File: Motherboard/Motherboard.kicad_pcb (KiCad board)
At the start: 8 copper layers, 304.8 x 243.8 mm, 102 parts, among them J1 ATX-20, J2 65SIB_Connector, J3 DB9_Header, J4 GPIO_Connector, J5 Expansion_Connector, J6 Expansion_Connector, J7 Expansion_Connector, J8 Expansion_Connector, J9 Expansion_Connector, SW1 SW_SPST, U1 74HCT138, U10 74HCT138, U2 AS6C4008-55PCN, U3 74HCT138, U4 74HCT138, U5 74HCT138, U6 28C010, U7 74HCT08, U8 74HCT138, U9 74HCT138, X1 ACO-8MHz

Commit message: 406 traces left to route...
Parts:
- added C3: 100 nF, Capacitor_THT:C_Disc_D3.0mm_W1.6mm_P2.50mm, F.Cu at (160.0, 108.0)
- added U11: 74HCT02, Package_DIP:DIP-14_W7.62mm_Socket_LongPads, F.Cu at (154.9, 114.3)
- J4: footprint Connector_PinSocket_2.54mm:PinSocket_2x11_P2.54mm_Vertical -> Connector_PinHeader_2.54mm:PinHeader_2x11_P2.54mm_Vertical
- moved J4 32.5 mm to (297.2, 223.5)
- renumbered NOR1 to NOT1
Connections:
- U10 pad 11: unconnected-(U10-Pad11) -> ~{CS_65SIB}
- U10 pad 13: ~{CS_65SIB} -> unconnected-(U10-Pad13)
- U2 pad 1: ROM4_EN -> RAM4_EN
- U2 pad 2: ROM2_EN -> RAM2_EN
- U2 pad 30: ROM3_EN -> RAM3_EN
- U2 pad 31: ROM1_EN -> RAM1_EN
- U4 pad 5: GND -> A7
- U4 pad 6: A7 -> VCC
- U7 pad 4: Net-(U7-Pad4) -> (no net)
- U7 pad 5: Net-(U7-Pad5) -> (no net)
- U7 pad 6: CS_DEV -> (no net)
- ~CS_DEV1 pad 10: Net-(U7-Pad5) -> Net-(U11-Pad3)
- ~CS_DEV2 pad 15: Net-(U7-Pad4) -> Net-(U11-Pad2)
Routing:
- net ~{IRQ1}: track 55.9 -> 411.3 mm, vias 1 -> 3
- net CLK: track 129.5 -> 375.8 mm, vias 3 -> 5
- net R\~{W}: track 39.4 -> 229.9 mm, vias 1 -> 2
- net A0: track 67.5 -> 223.1 mm, vias 1 -> 2
- net MEM_D0: track 158.0 -> 264.3 mm
- net MEM_D2: track 157.8 -> 263.8 mm
- net MEM_D1: track 157.9 -> 263.8 mm
- net PHI2: track 67.3 -> 139.5 mm, vias 2 -> 3
- net A3: track 63.7 -> 132.3 mm, vias 1 -> 2
- net A2: track 65.3 -> 127.5 mm, vias 1 -> 2
- net Net-(U11-Pad3): track 0.00 -> 62.2 mm, vias 0 -> 2
- net A1: track 66.2 -> 122.1 mm, vias 1 -> 2
- net VCC: track 1422.6 -> 1478.1 mm
- net CA1: track 37.3 -> 0.00 mm
- net CA2: track 33.5 -> 0.00 mm
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
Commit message: 405 unrouted traces...
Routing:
- net GPIO9: track 7.67 -> 0.00 mm
- net RAM1_EN: track 1.27 -> 0.00 mm
- net ROM4_EN: track 0.77 -> 0.00 mm
- net GND: track 1607.3 -> 1606.8 mm
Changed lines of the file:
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@@
   (segment (start 165.11 86.365) (end 165.11 96.525) (width 0.25) (layer "F.Cu") (net 1))
   (segment (start 102.88 96.51) (end 102.88 93.97) (width 0.25) (layer "F.Cu") (net 1))
-  (segment (start 119.39 124.45) (end 119.89904 124.45) (width 0.25) (layer "F.Cu") (net 1))
   (segment (start 162.575 99.06) (end 140.97 99.06) (width 0.25) (layer "F.Cu") (net 1))
   (segment (start 77.48 34.3) (end 61.17 34.3) (width 0.25) (layer "F.Cu") (net 1))
@@
   (segment (start 133.505489 210.664511) (end 143.625489 210.664511) (width 0.25) (layer "In3.Cu") (net 1))
   (segment (start 219.705 177.8) (end 220.829511 178.924511) (width 0.25) (layer "In3.Cu") (net 1))
-  (segment (start 234.95 143.51) (end 234.945 143.505) (width 0.25) (layer "F.Cu") (net 2))
-  (segment (start 234.945 143.505) (end 234.945 142.24) (width 0.25) (layer "F.Cu") (net 2))
-  (segment (start 265.43 141.6975) (end 264.8875 142.24) (width 0.25) (layer "In3.Cu") (net 9))
   (segment (start 251.46 110.49) (end 260.35 110.49) (width 0.25) (layer "In1.Cu") (net 20))
   (segment (start 144.79 111.75) (end 144.8 111.76) (width 0.25) (layer "In1.Cu") (net 20))
@@
   (segment (start 172.73 83.825) (end 179.065 83.825) (width 0.25) (layer "In3.Cu") (net 30))
   (segment (start 172.73 83.825) (end 172.73 85.08) (width 0.25) (layer "In5.Cu") (net 30))
-  (segment (start 138.44 85.08) (end 138.43 85.09) (width 0.25) (layer "In5.Cu") (net 30))
   (segment (start 172.73 85.08) (end 138.44 85.08) (width 0.25) (layer "In5.Cu") (net 30))
   (segment (start 138.44 85.08) (end 138.44 83.825) (width 0.25) (layer "In5.Cu") (net 30))
@@
   (segment (start 314.97 158.76) (end 314.96 158.75) (width 0.25) (layer "In2.Cu") (net 64))
   (segment (start 314.97 210.83) (end 314.97 158.76) (width 0.25) (layer "In2.Cu") (net 64))
-  (segment (start 266.1575 158.75) (end 285.75 158.75) (width 0.25) (layer "In3.Cu") (net 64))
+  (segment (start 266.1575 158.75) (end 314.96 158.75) (width 0.25) (layer "In3.Cu") (net 64))
   (segment (start 220.829511 158.604511) (end 263.762989 158.604511) (width 0.25) (layer "In3.Cu") (net 64))
   (segment (start 264.8875 157.48) (end 266.1575 158.75) (width 0.25) (layer "In3.Cu") (net 64))
   (segment (start 263.762989 158.604511) (end 264.8875 157.48) (width 0.25) (layer "In3.Cu") (net 64))
-  (segment (start 314.96 158.75) (end 285.75 158.75) (width 0.25) (layer "In3.Cu") (net 64))
   (segment (start 219.705 157.48) (end 220.829511 158.604511) (width 0.25) (layer "In3.Cu") (net 64))
   (via (at 312.42 156.21) (size 0.8) (drill 0.4) (layers "F.Cu" "B.Cu") (net 65))
   (segment (start 312.43 156.22) (end 312.43 210.83) (width 0.25) (layer "In2.Cu") (net 65))
   (segment (start 312.42 156.21) (end 312.43 156.22) (width 0.25) (layer "In2.Cu") (net 65))
-  (segment (start 266.1575 156.21) (end 285.75 156.21) (width 0.25) (layer "In3.Cu") (net 65))
-  (segment (start 285.75 156.21) (end 312.42 156.21) (width 0.25) (layer "In3.Cu") (net 65))
+  (segment (start 266.1575 156.21) (end 312.42 156.21) (width 0.25) (layer "In3.Cu") (net 65))
   (segment (start 264.8875 154.94) (end 266.1575 156.21) (width 0.25) (layer "In3.Cu") (net 65))
   (segment (start 263.762989 156.064511) (end 264.8875 154.94) (width 0.25) (layer "In3.Cu") (net 65))
@@
   (segment (start 309.88 153.67) (end 309.89 153.68) (width 0.25) (layer "In2.Cu") (net 66))
   (segment (start 309.89 153.68) (end 309.89 210.83) (width 0.25) (layer "In2.Cu") (net 66))
-  (segment (start 266.1575 153.67) (end 285.75 153.67) (width 0.25) (layer "In3.Cu") (net 66))
+  (segment (start 266.1575 153.67) (end 309.88 153.67) (width 0.25) (layer "In3.Cu") (net 66))
   (segment (start 219.705 152.4) (end 220.829511 153.524511) (width 0.25) (layer "In3.Cu") (net 66))
   (segment (start 220.829511 153.524511) (end 263.762989 153.524511) (width 0.25) (layer "In3.Cu") (net 66))
   (segment (start 264.8875 152.4) (end 266.1575 153.67) (width 0.25) (layer "In3.Cu") (net 66))
-  (segment (start 285.75 153.67) (end 309.88 153.67) (width 0.25) (layer "In3.Cu") (net 66))
   (segment (start 263.762989 153.524511) (end 264.8875 152.4) (width 0.25) (layer "In3.Cu") (net 66))
   (via (at 304.8 151.13) (size 0.8) (drill 0.4) (layers "F.Cu" "B.Cu") (net 67))
   (segment (start 304.81 210.83) (end 304.81 151.14) (width 0.25) (layer "In2.Cu") (net 67))
-  (segment (start 266.1575 151.13) (end 285.75 151.13) (width 0.25) (layer "In3.Cu") (net 67))
-  (segment (start 285.75 151.13) (end 304.8 151.13) (width 0.25) (layer "In3.Cu") (net 67))
+  (segment (start 266.1575 151.13) (end 304.8 151.13) (width 0.25) (layer "In3.Cu") (net 67))
   (segment (start 219.705 149.86) (end 220.829511 150.984511) (width 0.25) (layer "In3.Cu") (net 67))
   (segment (start 220.829511 150.984511) (end 263.762989 150.984511) (width 0.25) (layer "In3.Cu") (net 67))
@@
   (segment (start 105.41 166.37) (end 213.36 166.37) (width 0.25) (layer "In3.Cu") (net 86))
   (segment (start 213.36 166.37) (end 213.36 55.88) (width 0.25) (layer "In4.Cu") (net 86))
-  (segment (start 274.295 214.655) (end 274.315 214.635) (width 0.25) (layer "In3.Cu") (net 88))
-  (segment (start 271.78 224.79) (end 271.755 224.815) (width 0.25) (layer "In2.Cu") (net 96))
-  (segment (start 271.78 232.42) (end 271.78 224.79) (width 0.25) (layer "In2.Cu") (net 96))
   (segment (start 300.98 257.815) (end 300.99 257.825) (width 0.25) (layer "In3.Cu") (net 105))
   (segment (start 289.555 257.815) (end 300.98 257.815) (width 0.25) (layer "In3.Cu") (net 105))
@@
   (via (at 130.81 50.8) (size 0.8) (drill 0.4) (layers "F.Cu" "B.Cu") (net 112))
   (segment (start 130.81 40.64) (end 130.81 50.8) (width 0.25) (layer "In2.Cu") (net 112))
-  (segment (start 130.81 50.8) (end 130.82 50.79) (width 0.25) (layer "In2.Cu") (net 112))
   (segment (start 138.43 50.8) (end 138.44 50.79) (width 0.25) (layer "In3.Cu") (net 112))
   (segment (start 130.81 50.8) (end 138.43 50.8) (width 0.25) (layer "In3.Cu") (net 112))

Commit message: 357 traces left to route...
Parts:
- added G***: LOGO, WolfNet:WolfNet-Logo_silkscreen, F.Cu at (170.2, 137.2)
- added REF**: CE-Logo_16.8x12mm_SilkScreen, Symbol:CE-Logo_16.8x12mm_SilkScreen, F.Cu at (123.2, 162.6)
- added REF**: OSHW-Logo_11.4x12mm_SilkScreen, Symbol:OSHW-Logo_11.4x12mm_SilkScreen, F.Cu at (157.5, 162.6)
- added REF**: RoHS-Logo_12mm_SilkScreen, Symbol:RoHS-Logo_12mm_SilkScreen, F.Cu at (135.9, 175.3)
- added REF**: KiCad-Logo2_12mm_SilkScreen, Symbol:KiCad-Logo2_12mm_SilkScreen, F.Cu at (180.3, 161.3)
- added REF**: ESD-Logo_13.2x12mm_SilkScreen, Symbol:ESD-Logo_13.2x12mm_SilkScreen, F.Cu at (142.2, 162.6)
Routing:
- net A2: track 127.5 -> 235.0 mm
- net A3: track 132.3 -> 238.5 mm
- net MEM_D6: track 157.8 -> 264.0 mm
- net ~{RESET}: track 0.00 -> 106.2 mm
- net MEM_D7: track 158.0 -> 264.2 mm
- net A6: track 148.8 -> 255.0 mm
- net A4: track 148.8 -> 255.0 mm
- net MEM_D5: track 158.0 -> 264.2 mm
- net A1: track 122.1 -> 228.2 mm
- net MEM_D3: track 157.8 -> 263.8 mm
- net A5: track 148.8 -> 254.9 mm
- net MEM_D4: track 157.8 -> 263.7 mm
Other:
- board text added: "An Open-Source Hardware project. Released for FREE under the Solderpad Hardware License v2.1"
- board text added: "WolfNet-6502-WBC"
- board text added: "https://github.com/TheAlmostGenius/WolfNet-6502-WBC"
- board text added: "https://thealmostgenius.geekgalaxy.com/WolfNet-6502-WBC/"

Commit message: 316 traces left to route...
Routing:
- net A7: track 146.2 -> 376.3 mm, vias 1 -> 3
- net A8: track 0.00 -> 152.5 mm
- net A9: track 0.00 -> 152.3 mm
- net A5: track 254.9 -> 366.9 mm, vias 1 -> 3
- net PHI1: track 0.00 -> 106.2 mm
- net VCC: track 1478.1 -> 1576.7 mm
- net PHI2: track 139.5 -> 219.3 mm
- net CLK: track 375.8 -> 455.6 mm
- net ~{IRQ3}: track 43.2 -> 119.4 mm, vias 1 -> 3
- net GND: track 1606.8 -> 1666.5 mm
- net A11: track 0.00 -> 46.2 mm
- net A10: track 0.00 -> 46.2 mm
- net A6: track 255.0 -> 297.7 mm, vias 1 -> 2
- net A4: track 255.0 -> 292.1 mm, vias 1 -> 2

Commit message: 311 traces to route...
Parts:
- moved J4 2.55 mm to (299.7, 223.5)
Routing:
- net R\~{W}: track 229.9 -> 323.8 mm, vias 2 -> 5
- net GND: track 1666.5 -> 1754.1 mm
- net CB2: track 0.00 -> 31.8 mm, vias 0 -> 4
- net VCC: track 1576.7 -> 1594.0 mm
- net GPIO0: track 0.00 -> 12.7 mm, vias 0 -> 1
- net GPIO2: track 0.00 -> 10.2 mm, vias 0 -> 1
- net GPIO1: track 0.00 -> 7.63 mm, vias 0 -> 1
- net GPIO6: track 0.00 -> 6.35 mm
- net GPIO4: track 0.00 -> 6.35 mm
- net GPIO12: track 0.00 -> 6.35 mm
- net GPIO10: track 0.00 -> 6.35 mm
- net CB1: track 0.00 -> 6.35 mm
- net CA1: track 0.00 -> 6.35 mm
- net GPIO8: track 0.00 -> 6.35 mm
- net GPIO14: track 0.00 -> 6.35 mm
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
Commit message: 290 unrouted traces...
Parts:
- moved J4 38.6 mm to (262.9, 212.1)
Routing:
- net A0: track 223.1 -> 318.4 mm, vias 2 -> 5
- net A1: track 228.2 -> 323.5 mm, vias 2 -> 5
- net CA2: track 2.54 -> 82.4 mm, vias 0 -> 1
- net CA1: track 6.35 -> 79.6 mm, vias 0 -> 1
- net GND: track 1754.1 -> 1718.1 mm
- net GPIO15: track 2.54 -> 26.0 mm
- net GPIO13: track 2.54 -> 23.5 mm
- net GPIO11: track 2.54 -> 21.1 mm
- net GPIO9: track 2.54 -> 18.5 mm
- net CB1: track 6.35 -> 22.2 mm
- net GPIO14: track 6.35 -> 21.5 mm
- net GPIO7: track 2.54 -> 15.9 mm
- net GPIO12: track 6.35 -> 18.9 mm
- net GPIO5: track 2.54 -> 14.6 mm
- net GPIO10: track 6.35 -> 16.4 mm
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
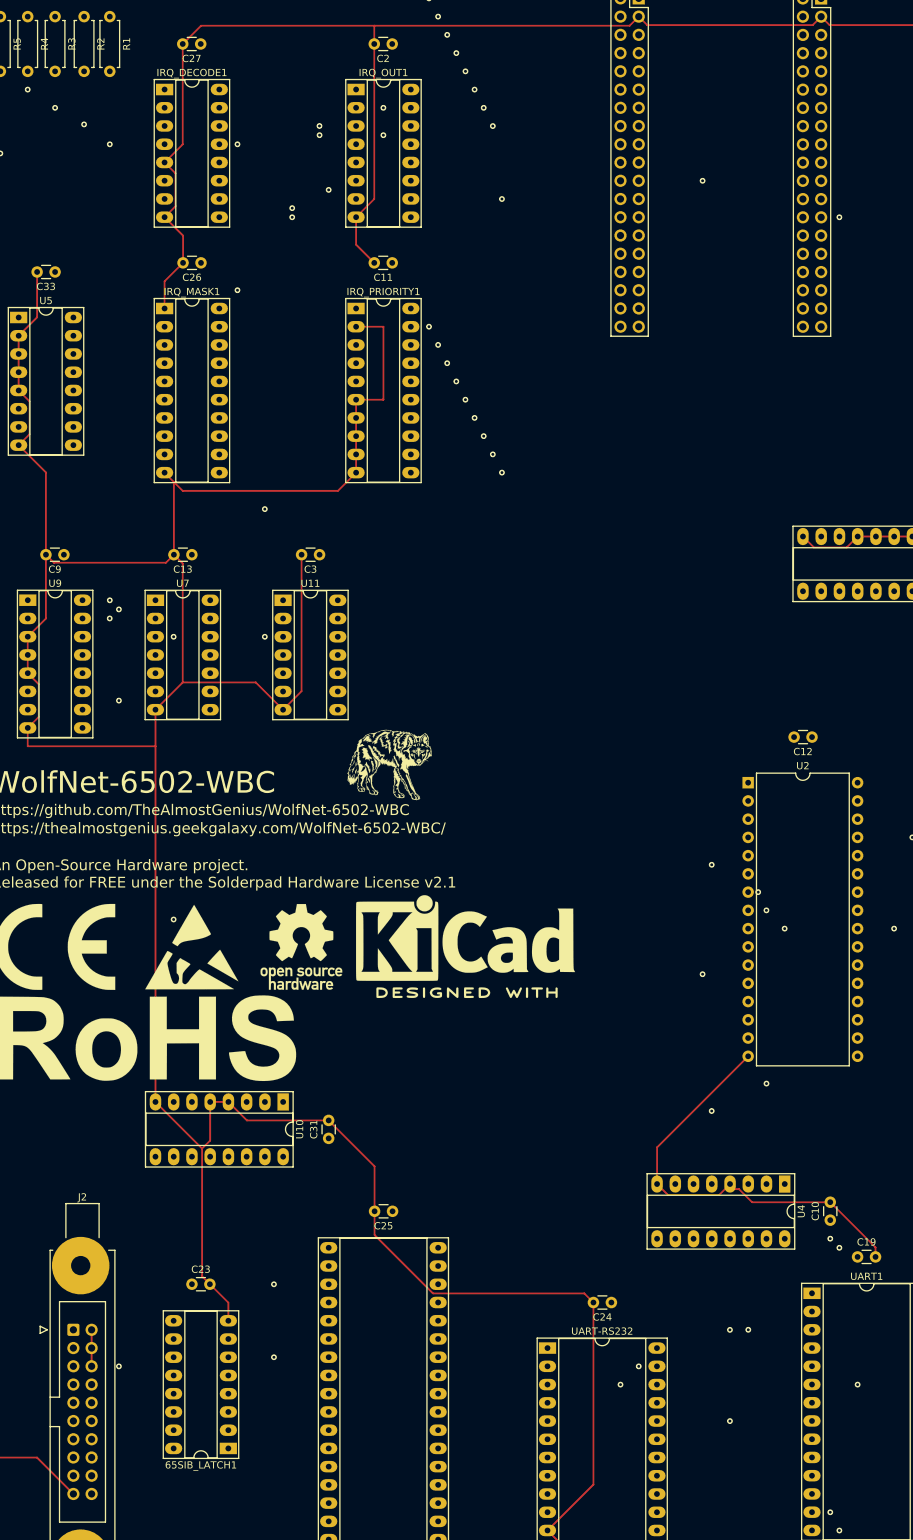
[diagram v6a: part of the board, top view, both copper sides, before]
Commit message: 286 unrouted traces...
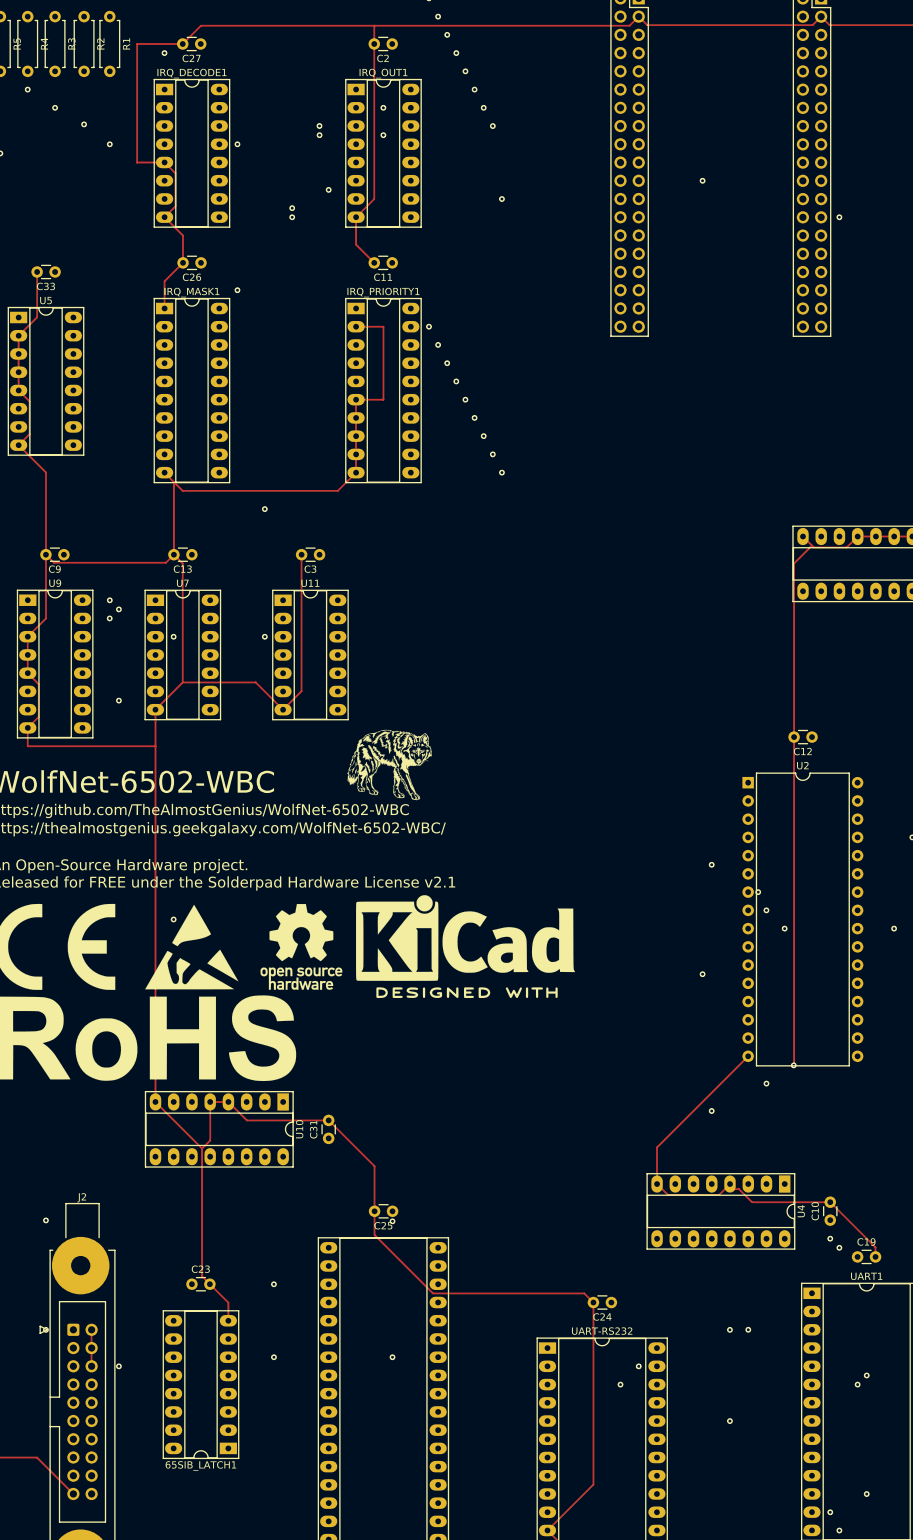
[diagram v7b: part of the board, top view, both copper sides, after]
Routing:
- net ~{CONF}: track 0.00 -> 92.7 mm, vias 0 -> 4
- net GND: track 1718.1 -> 1800.7 mm, vias 0 -> 1
- net VCC: track 1588.9 -> 1649.6 mm
- net DSR_COM: track 0.00 -> 53.9 mm, vias 0 -> 2
- net ~{IRQ4}: track 21.6 -> 26.7 mm, vias 1 -> 2

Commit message: 257 unrouted traces...
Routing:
- net A1: track 323.5 -> 568.0 mm, vias 5 -> 9
- net A0: track 318.4 -> 557.2 mm, vias 5 -> 9
- net MEM_D5: track 264.2 -> 349.2 mm
- net MEM_D1: track 263.8 -> 347.9 mm
- net MEM_D7: track 264.2 -> 348.3 mm
- net MEM_D6: track 264.0 -> 348.1 mm
- net PHI2: track 219.3 -> 303.3 mm
- net MEM_D4: track 263.7 -> 347.7 mm
- net MEM_D3: track 263.8 -> 347.8 mm
- net MEM_D0: track 264.3 -> 348.3 mm
- net DSR_COM_PORT: track 0.00 -> 52.7 mm
- net ~{65SIB_IRQ}: track 0.00 -> 50.6 mm
- net GND: track 1800.7 -> 1839.4 mm
- net DCD_COM_PORT: track 0.00 -> 37.8 mm
- net RTS_COM_PORT: track 0.00 -> 33.9 mm
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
